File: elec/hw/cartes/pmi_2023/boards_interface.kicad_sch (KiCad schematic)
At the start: 2 parts

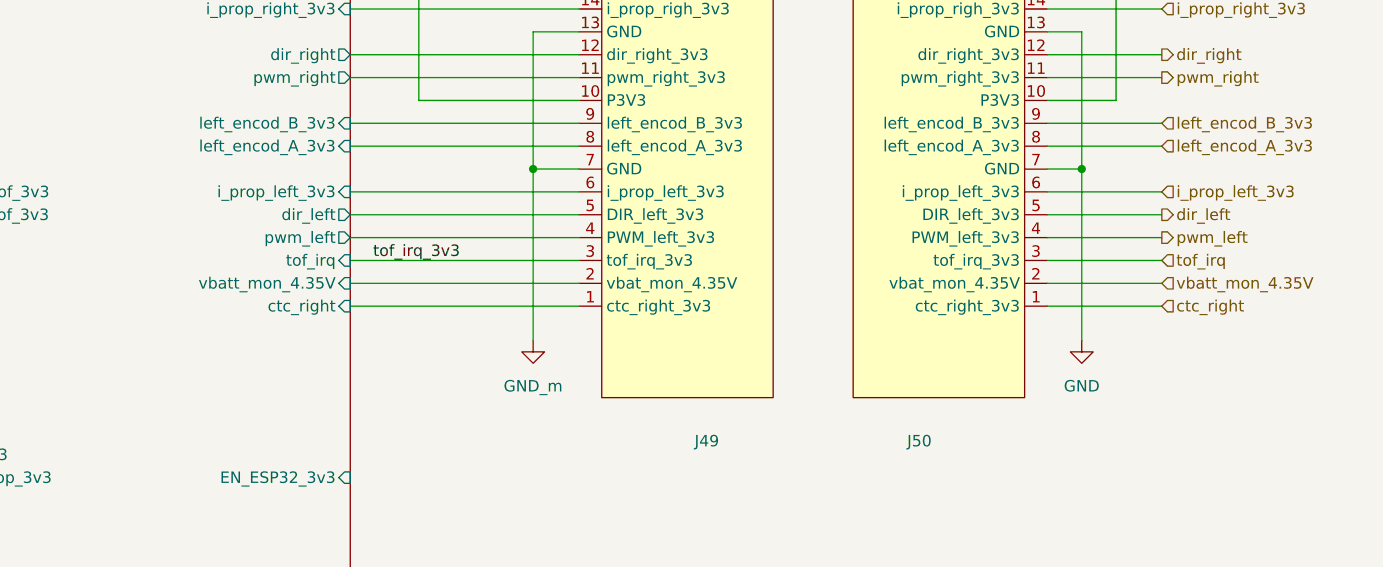
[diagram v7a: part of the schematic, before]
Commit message: routing cleanup, test points added to allow charging of battery in the pmi
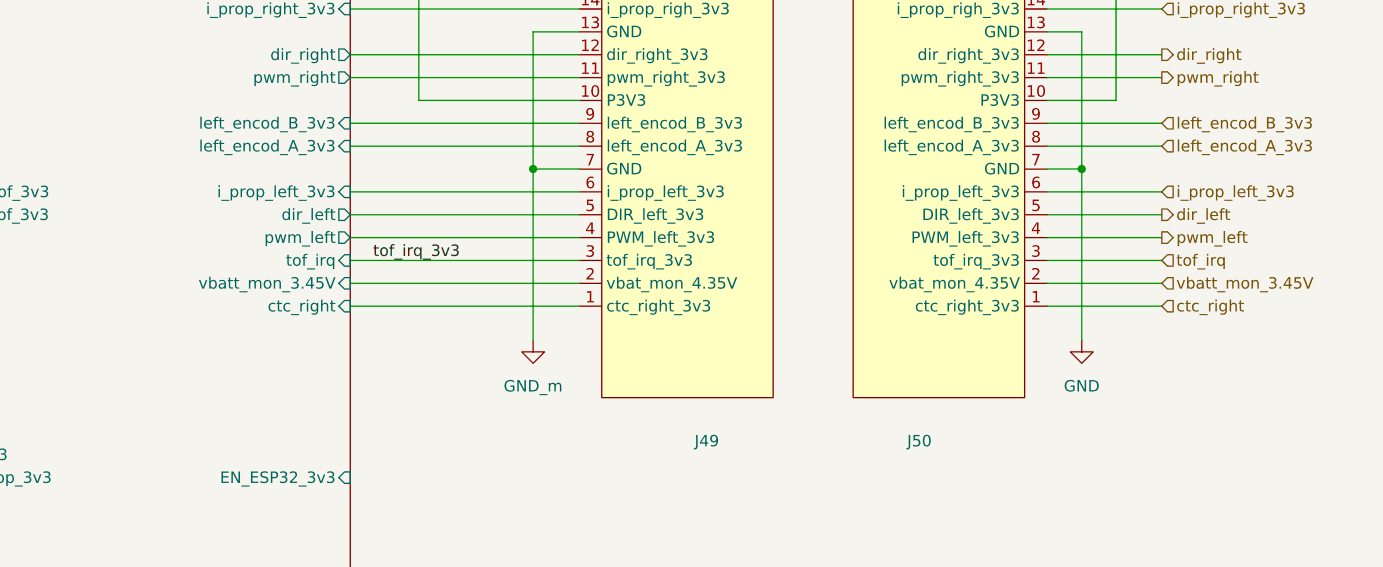
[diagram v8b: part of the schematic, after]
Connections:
- net com/vbatt_mon_4.35V renamed com/vbatt_mon_3.45V
- net vbatt_mon_4.35V renamed vbatt_mon_3.45V
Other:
- sheet com ports: added vbatt_mon_3.45V; removed vbatt_mon_4.35V
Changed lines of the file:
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@@
 		)
 	)
-	(hierarchical_label "vbatt_mon_4.35V"
+	(hierarchical_label "vbatt_mon_3.45V"
 		(shape input)
 		(at 256.54 107.95 0)
@@
 			)
 		)
-		(pin "vbatt_mon_4.35V" input
+		(pin "vbatt_mon_3.45V" input
 			(at 166.37 107.95 0)
 			(effects
